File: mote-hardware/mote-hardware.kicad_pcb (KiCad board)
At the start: 2 copper layers, 93.6 x 102.8 mm, 87 parts, among them J1 USB_C_Receptacle_USB2.0_14P, J2 JST_XH2.54-SP, J4 SM03B-SRSS-TB, J5 Conn_01x03_Pin, J6 Conn_01x03_Pin, J7 JST_PH_B6B, J8 JST_PH_B6B, SW1 SW_Push, SW2 SW_Push, U1 RP2354_60QFN, U2 NCP1117-3.3_SOT223, U4 RP Radio Module 2, U5 DRV8833PW, U9 LSM6DS3, Y1 ABM8-272-T3

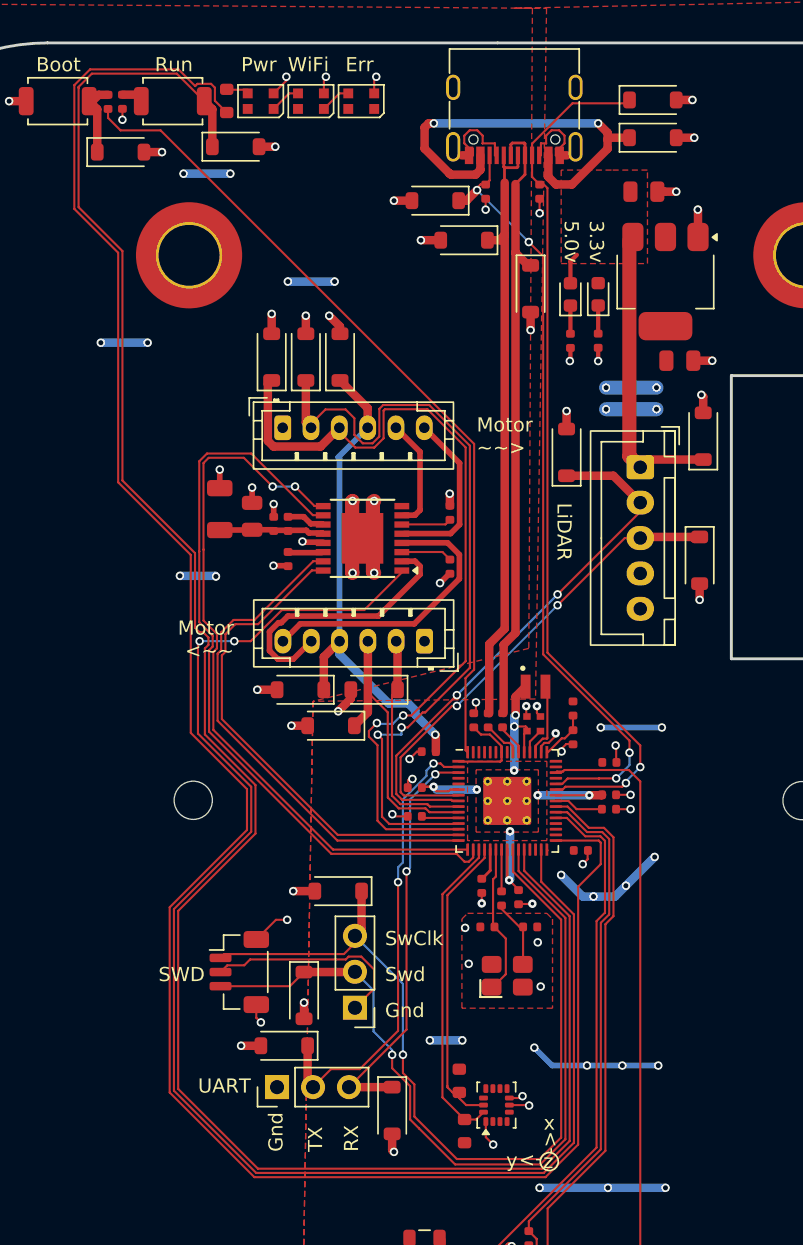
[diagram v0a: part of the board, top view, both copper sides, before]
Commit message: mote-hardware v0.2.0 (#63)
Improvements to the pcb design for rev v0.2.0
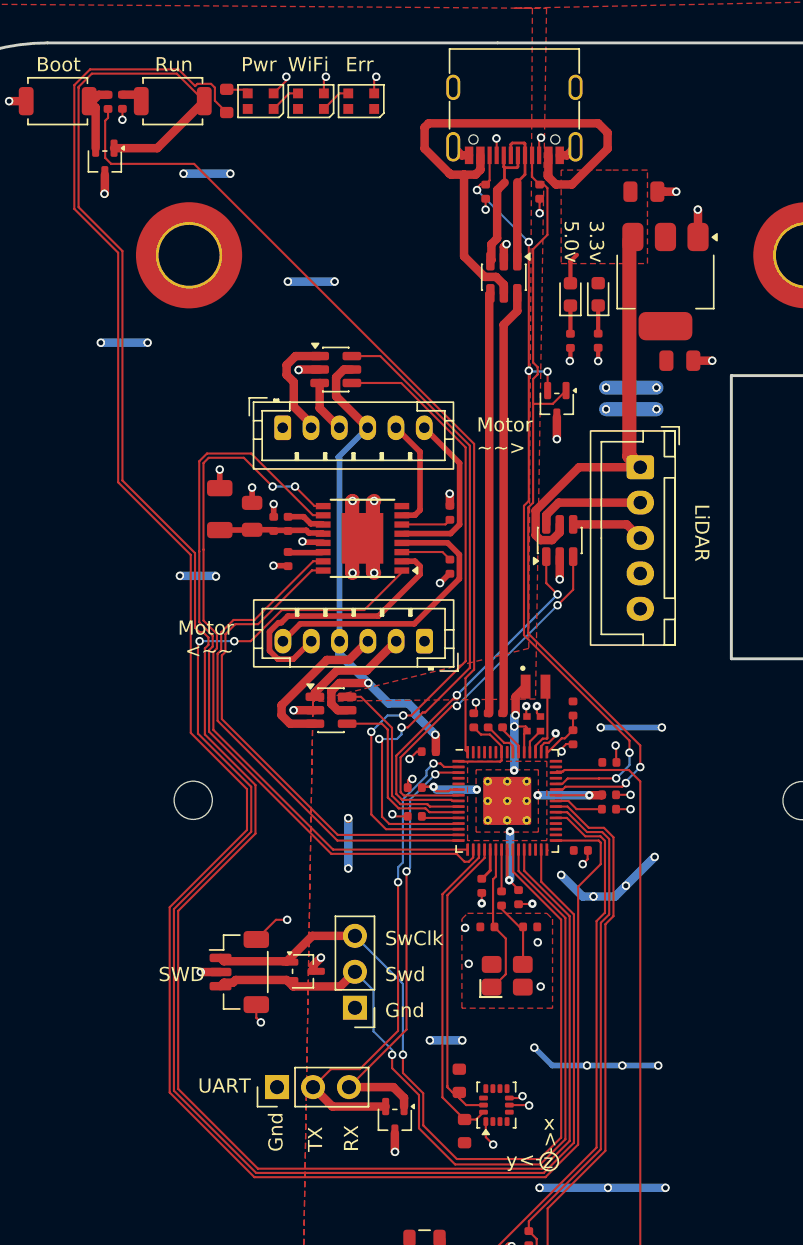
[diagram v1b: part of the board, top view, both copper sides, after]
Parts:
- removed D10, D11, D14, D15, D16, D17, D18, D19, D20, D21, D22, D23, D6, D7, D8, D9: PTVS5V0S1UR-FS, Diode_SMD:D_SOD-123
- removed D12, D13, D24, D25: PTVS6V0S1UR, Diode_SMD:D_SOD-123
- added U10: TPD2E2U06DCK, Package_TO_SOT_SMD:SOT-323_SC-70, F.Cu at (103.6, 65.0)
- added U11: USBLC6-2SC6, Package_TO_SOT_SMD:SOT-23-6, F.Cu at (87.6, 86.7)
- added U12: USBLC6-2SC6, Package_TO_SOT_SMD:SOT-23-6, F.Cu at (88.0, 62.6)
- added U13: TPD2E2U06DCK, Package_TO_SOT_SMD:SOT-323_SC-70, F.Cu at (71.7, 47.9)
- added U3: USBLC6-2SC6, Package_TO_SOT_SMD:SOT-23-6, F.Cu at (99.8, 56.1)
- added U6: TPD2E2U06DCK, Package_TO_SOT_SMD:SOT-323_SC-70, F.Cu at (85.6, 105.1)
- added U7: TPD2E2U06DCK, Package_TO_SOT_SMD:SOT-323_SC-70, F.Cu at (92.1, 115.6)
- added U8: USBLC6-2SC6, Package_TO_SOT_SMD:SOT-23-6, F.Cu at (103.8, 74.7)
- H5, H6: footprint MountingHole:MountingHole_4.3mm_M4_DIN965_Pad_TopOnly -> mote-hardware:MountingHole_4.3mm_M4_DIN965_Pad_TopOnly
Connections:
- J1 pad A6: /USB_D+ -> Net-(J1-D+-PadA6)
- J1 pad A7: /USB_D- -> Net-(J1-D--PadA7)
- J1 pad B6: /USB_D+ -> Net-(J1-D+-PadA6)
- J1 pad B7: /USB_D- -> Net-(J1-D--PadA7)
- J2 pad 2: /lidar_rx -> Net-(J2-Pin_2)
- J2 pad 3: /lidar_tx -> Net-(J2-Pin_3)
- J7 pad 2: /motor_left_encoder_a -> /motors/left_encoder_a_internal
- J7 pad 3: /motor_left_encoder_b -> /motors/left_encoder_b_internal
- J8 pad 2: /motor_right_encoder_a -> /motors/right_encoder_a_internal
- J8 pad 3: /motor_right_encoder_b -> /motors/right_encoder_b_internal
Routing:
- net GND: track 118.5 -> 79.5 mm, vias 72 -> 63
- net /+5v: track 73.4 -> 90.2 mm, vias 10 -> 8
- net /USB_D-: track 44.1 -> 30.0 mm
- net /motor_right_encoder_b: track 59.8 -> 46.2 mm
- net /USB_D+: track 43.0 -> 29.7 mm
- net /lidar_rx: track 38.2 -> 26.4 mm
- net /motors/left_encoder_b_internal: track 0.00 -> 11.3 mm
- net Net-(J1-D--PadA7): track 0.00 -> 10.4 mm
- net /motor_left_encoder_b: track 23.5 -> 13.3 mm
- net /motor_right_encoder_a: track 56.5 -> 46.6 mm
- net Net-(J1-D+-PadA6): track 0.00 -> 9.70 mm
- net /lidar_tx: track 34.6 -> 26.1 mm
- net /motors/left_encoder_a_internal: track 0.00 -> 7.96 mm
- net Net-(J2-Pin_2): track 0.00 -> 7.66 mm
- net /motors/right_encoder_a_internal: track 0.00 -> 7.47 mm
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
